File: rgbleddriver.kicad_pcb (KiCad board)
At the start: 2 copper layers, 65.1 x 46.1 mm, 29 parts, among them J1 Screw_Terminal_01x02, J2 Screw_Terminal_01x06, J4 Conn_01x04, U1 PT4115, U2 PT4115, U3 PT4115

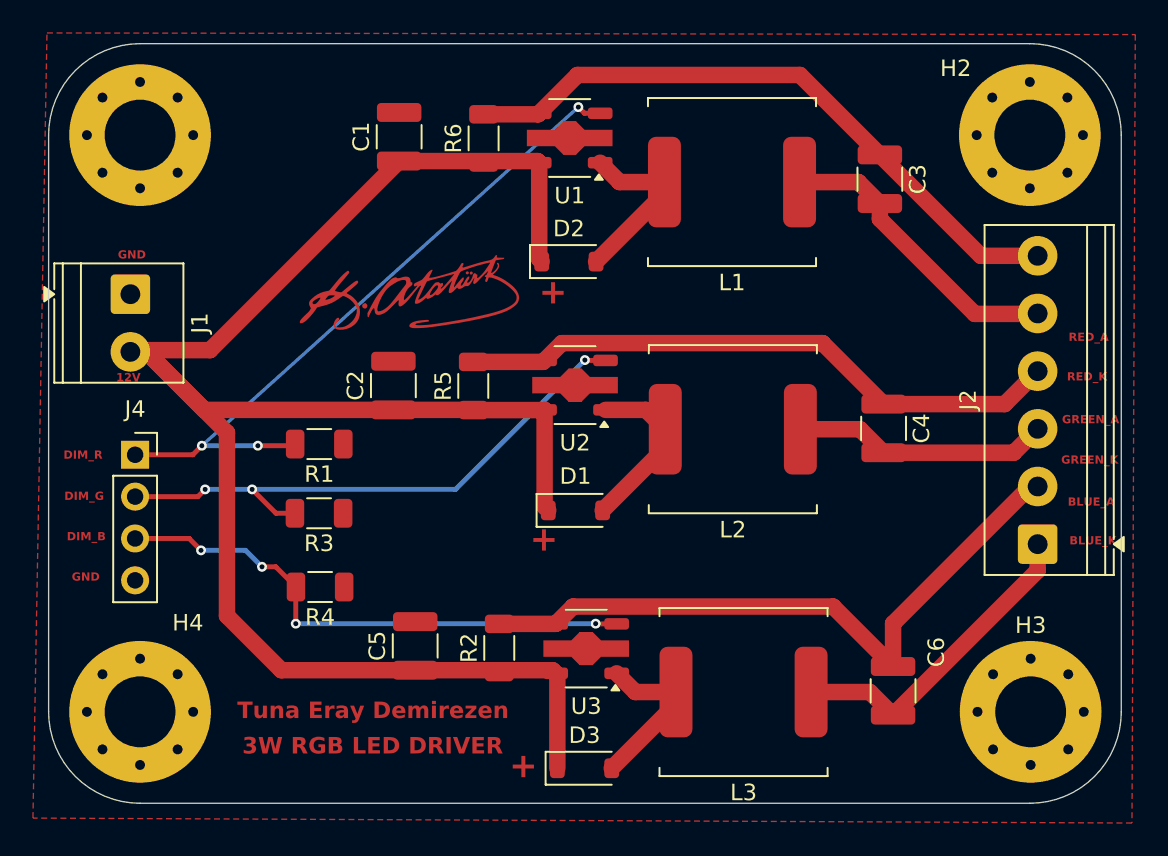
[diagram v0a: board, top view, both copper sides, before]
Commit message: Update revised RGB LED driver PCB files
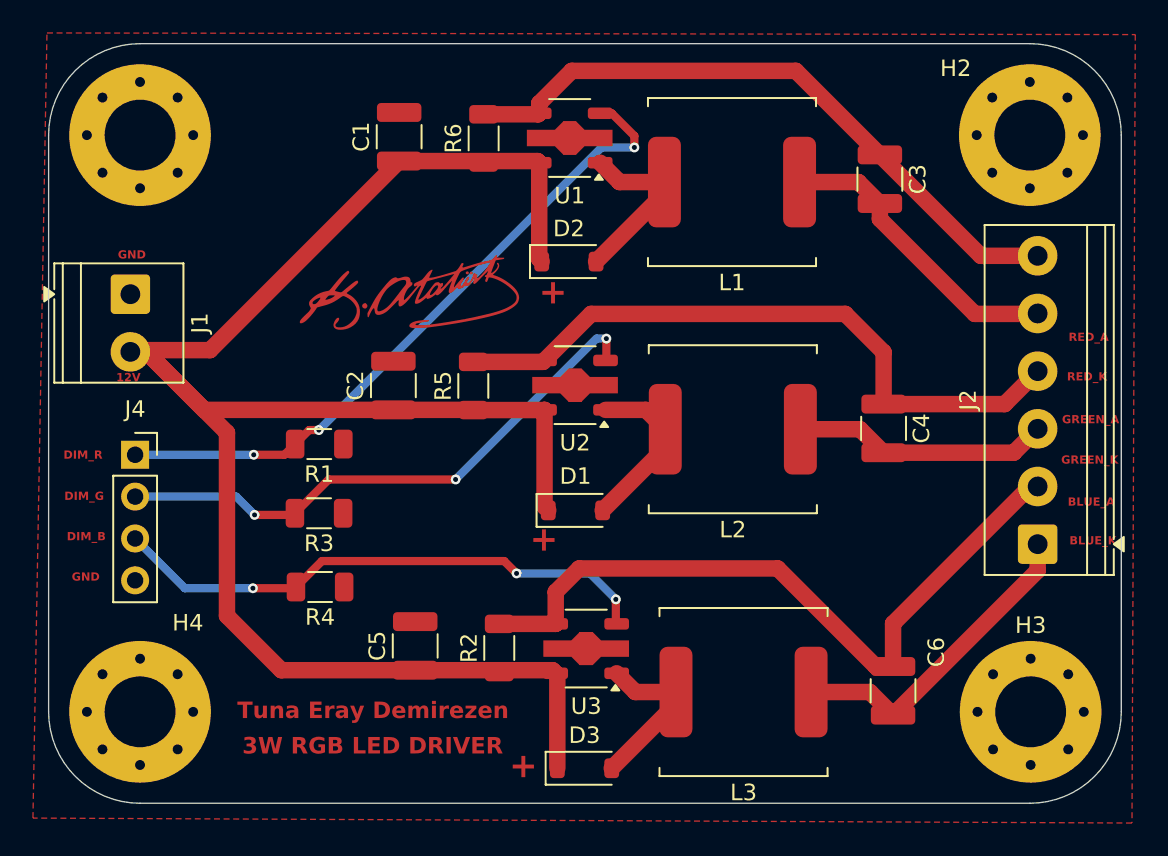
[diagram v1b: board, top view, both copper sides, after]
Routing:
- net DIM_R: track 11.5 -> 41.5 mm
- net GREEN_A: track 37.1 -> 40.4 mm
- net BLUE_A: track 40.7 -> 43.7 mm
- net DIM_B: track 32.8 -> 33.6 mm, vias 4 -> 3
- net RED_A: track 39.2 -> 39.7 mm
